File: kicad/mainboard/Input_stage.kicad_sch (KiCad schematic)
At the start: 46 parts, among them J10 Conn 1x4, J2 REMOTE INPUT, J4 MIC INPUT, J5 LINE INPUT, U2 LM324N, U4 LM358N

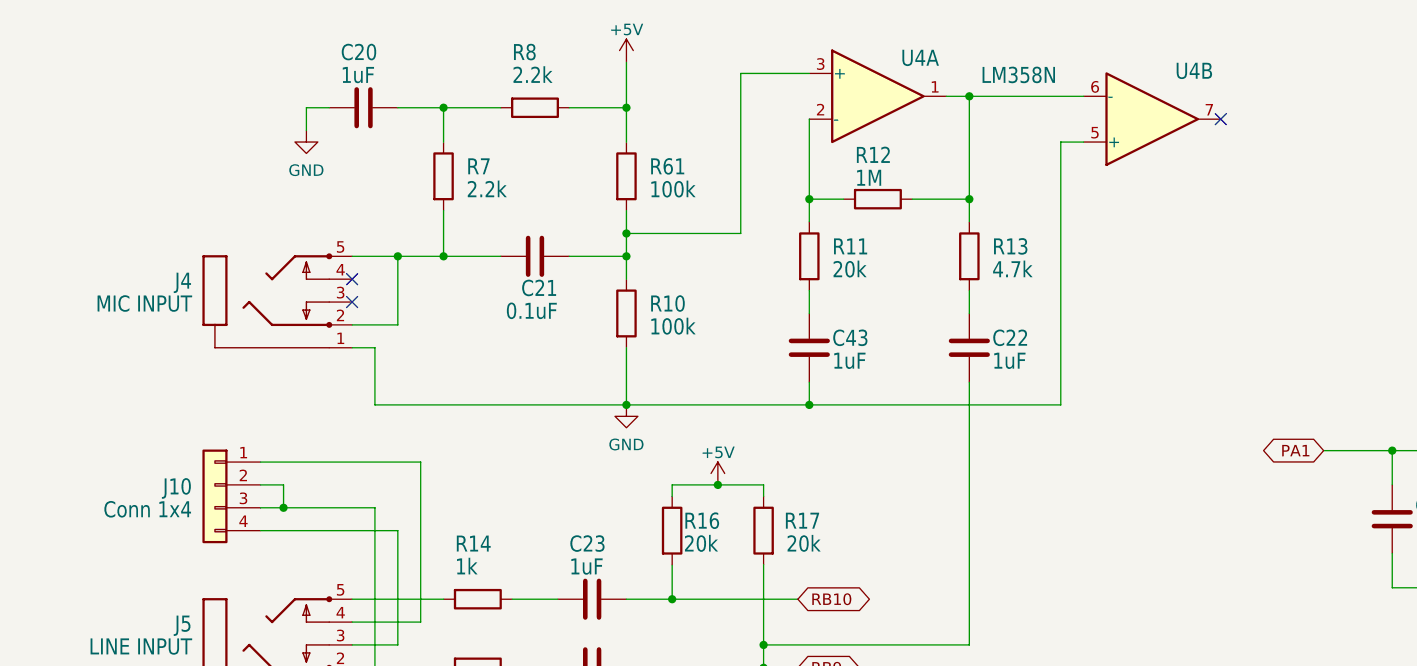
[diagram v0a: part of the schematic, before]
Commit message: Bringing mainboard up to par with V1.4 schematics based on images. Rerouted a few lines since they could not pass below the MOSFETs due to a different footprint/pad size.
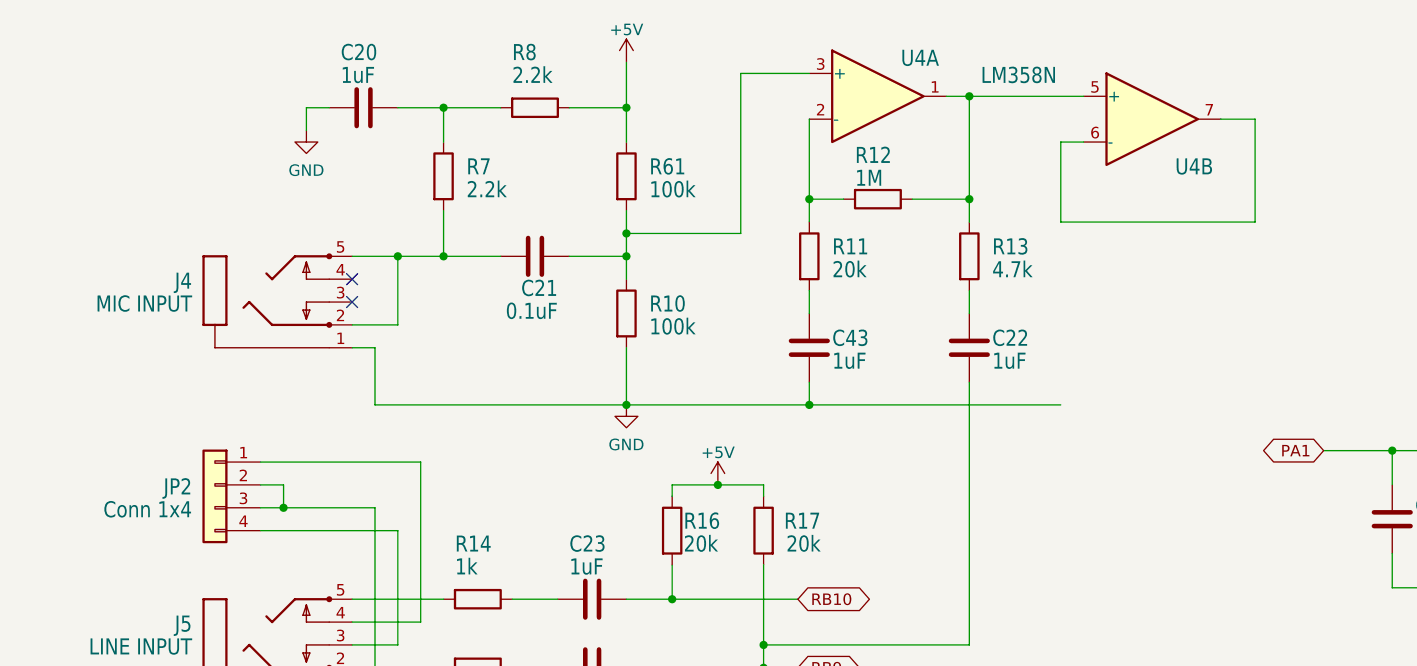
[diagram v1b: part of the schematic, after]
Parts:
- renumbered J10 to JP2
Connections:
- net GND: no longer U4.5 (+)
- net at R12.1, R13.1, U4.1: now also U4.5 (+); no longer U4.6 (-)
- net at U4.7: now also U4.6 (-)
- no-connect marks 5 -> 4
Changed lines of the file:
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@@
   (no_connect (at 50.8 50.8))
   (no_connect (at 50.8 48.26))
-  (no_connect (at 147.32 30.48))
   (wire (pts (xy 60.96 29.21) (xy 67.31 29.21))
     (stroke (width 0) (type default) (color 0 0 0 0))
@@
     (stroke (width 0) (type default) (color 0 0 0 0))
   )
+  (wire (pts (xy 151.13 41.91) (xy 151.13 30.48))
+    (stroke (width 0) (type default) (color 0 0 0 0))
+  )
   (wire (pts (xy 53.34 93.98) (xy 53.34 96.52))
     (stroke (width 0) (type default) (color 0 0 0 0))
@@
     (stroke (width 0) (type default) (color 0 0 0 0))
   )
+  (wire (pts (xy 147.32 30.48) (xy 151.13 30.48))
+    (stroke (width 0) (type default) (color 0 0 0 0))
+  )
+  (wire (pts (xy 129.54 41.91) (xy 151.13 41.91))
+    (stroke (width 0) (type default) (color 0 0 0 0))
+  )
   (wire (pts (xy 55.88 76.2) (xy 55.88 88.9))
     (stroke (width 0) (type default) (color 0 0 0 0))
@@
     (stroke (width 0) (type default) (color 0 0 0 0))
   )
-  (wire (pts (xy 129.54 33.02) (xy 129.54 62.23))
-    (stroke (width 0) (type default) (color 0 0 0 0))
-  )
   (wire (pts (xy 50.8 91.44) (xy 60.96 91.44))
     (stroke (width 0) (type default) (color 0 0 0 0))
@@
   )
   (wire (pts (xy 60.96 40.64) (xy 60.96 45.72))
+    (stroke (width 0) (type default) (color 0 0 0 0))
+  )
+  (wire (pts (xy 129.54 33.02) (xy 129.54 41.91))
     (stroke (width 0) (type default) (color 0 0 0 0))
   )
@@
     (pin "1")
   )
-  (symbol (lib_id "Amplifier_Operational:LM358") (at 139.7 30.48 0) (mirror x) (unit 2)
-    (in_bom yes) (on_board yes)
-    (property "Reference" "U4" (id 0) (at 142.24 24.13 0)
-      (effects (font (size 1.778 1.5113)) (justify left bottom))
-    )
-    (property "Value" "LM358N" (id 1) (at 142.24 25.4 0)
+  (symbol (lib_id "Amplifier_Operational:LM358") (at 139.7 30.48 0) (unit 2)
+    (in_bom yes) (on_board yes)
+    (property "Reference" "U4" (id 0) (at 142.24 36.83 0)
+      (effects (font (size 1.778 1.5113)) (justify left bottom))
+    )
+    (property "Value" "LM358N" (id 1) (at 142.24 35.56 0)
       (effects (font (size 1.778 1.5113)) (justify left bottom) hide)
     )
@@
   (symbol (lib_id "Connector_Generic:Conn_01x04") (at 35.56 71.12 0) (mirror y) (unit 1)
     (in_bom yes) (on_board yes)
-    (property "Reference" "J10" (id 0) (at 33.02 72.39 0)
-      (effects (font (size 1.778 1.5113)) (justify left bottom))
-    )
+    (property "Reference" "JP2" (id 0) (at 33.02 72.39 0)
+      (effects (font (size 1.778 1.5113)) (justify left bottom))
+    )

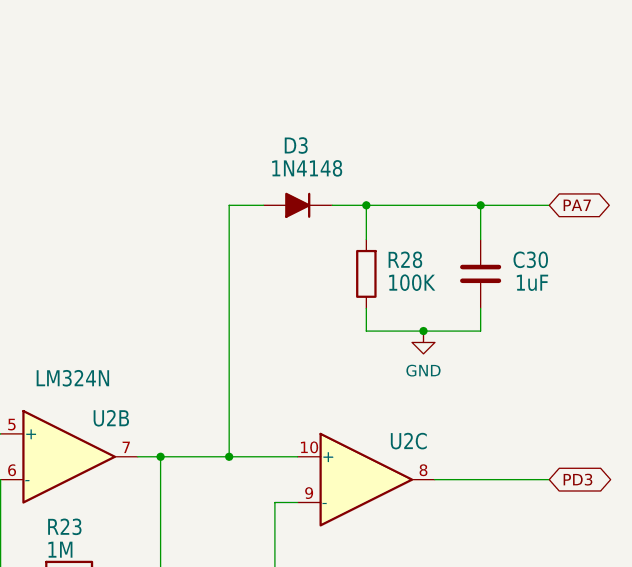
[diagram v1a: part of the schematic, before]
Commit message: Brought component numbers back in line with the original schematics
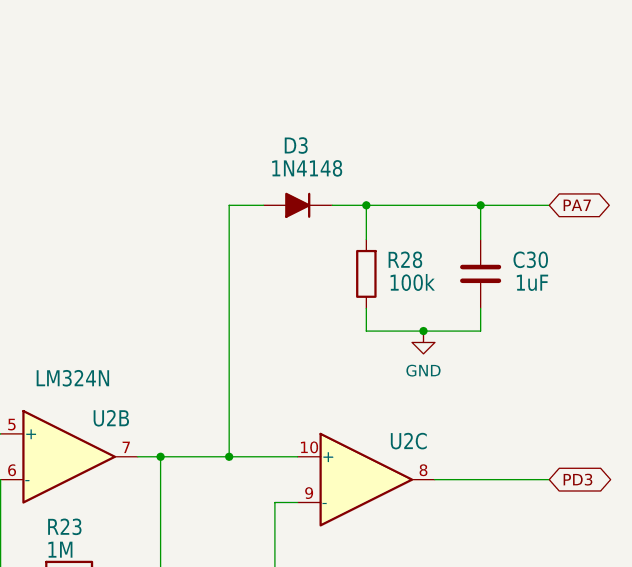
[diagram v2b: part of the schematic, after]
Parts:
- R28: value 100K -> 100k
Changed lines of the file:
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@@
       (effects (font (size 1.778 1.5113)) (justify left bottom))
     )
-    (property "Value" "100K" (id 1) (at 245.11 49.53 0)
+    (property "Value" "100k" (id 1) (at 245.11 49.53 0)
       (effects (font (size 1.778 1.5113)) (justify left bottom))
     )

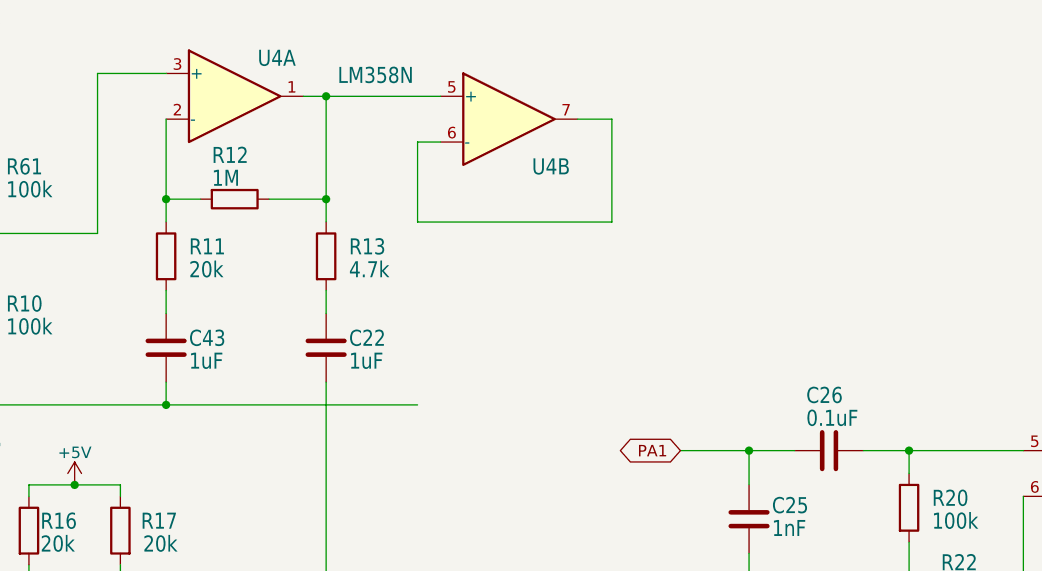
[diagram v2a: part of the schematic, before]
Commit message: A bit of cleanup, showing type of some OpAmps and clarification of wiring around U4
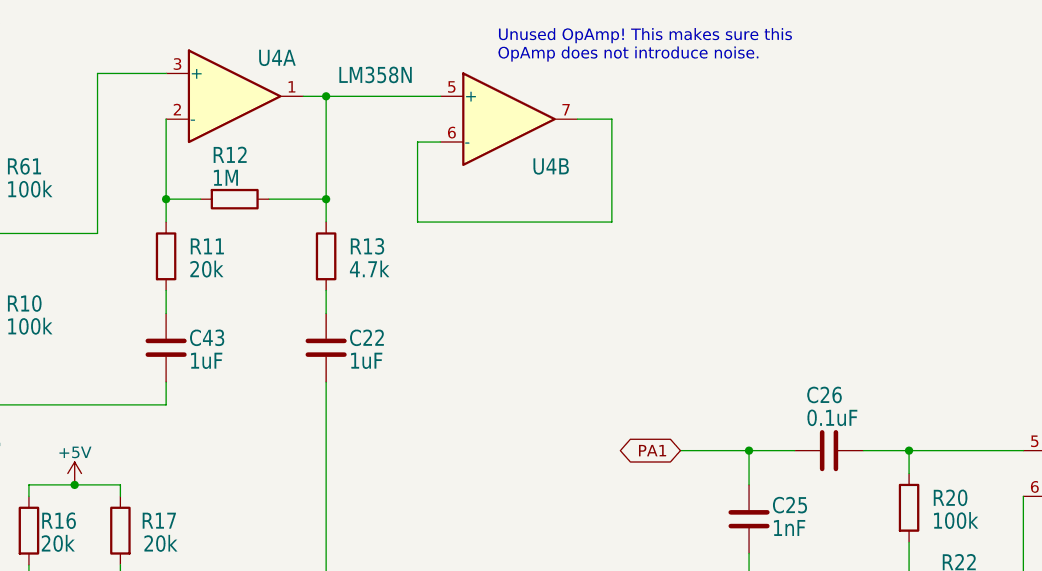
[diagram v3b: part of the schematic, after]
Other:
- note added: "Unused OpAmp! This makes sure this OpAmp does not introduce noise."
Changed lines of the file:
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@@
   (junction (at 101.6 39.37) (diameter 0) (color 0 0 0 0)
-  )
-  (junction (at 101.6 62.23) (diameter 0) (color 0 0 0 0)
   )
   (junction (at 243.84 142.24) (diameter 0) (color 0 0 0 0)
@@
     (stroke (width 0) (type default) (color 0 0 0 0))
   )
-  (wire (pts (xy 101.6 62.23) (xy 129.54 62.23))
-    (stroke (width 0) (type default) (color 0 0 0 0))
-  )
   (wire (pts (xy 184.15 67.31) (xy 179.07 67.31))
     (stroke (width 0) (type default) (color 0 0 0 0))
@@
     (stroke (width 0) (type default) (color 0 0 0 0))
   )
+  (text "Unused OpAmp! This makes sure this\nOpAmp does not introduce noise."
+    (at 138.43 24.13 0)
+    (effects (font (size 1.27 1.27)) (justify left bottom))
+  )
   (global_label "PD2" (shape bidirectional) (at 257.81 113.03 0) (fields_autoplaced)
